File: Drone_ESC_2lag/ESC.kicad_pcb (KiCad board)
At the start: 4 copper layers, 107 parts, among them IC1 STSPIN32G4, J1 Conn_02x05_Odd_Even, J2 Conn_01x02_Pin, J3 Conn_01x02_Pin, J4 Conn_01x03_Pin, P1 USB_C_Plug_USB2.0, Q1 STL130N6F7, Q2 STL130N6F7, Q3 STL130N6F7, Q4 STL130N6F7, Q5 STL130N6F7, Q6 STL130N6F7, SW1 JS102011SAQN, Y1 24.000MHz

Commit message: delt igennem VS
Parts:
- moved IC1 2.98 mm to (171.1, 51.5)
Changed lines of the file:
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@@
 	(footprint "Drone_ESC:QFN50P900X900X100-65N-D"
 		(layer "F.Cu")
-		(at 168.5375 53.095)
+		(at 171.05 51.5)
 		(descr "STSPIN32G4")
 		(tags "Integrated Circuit")

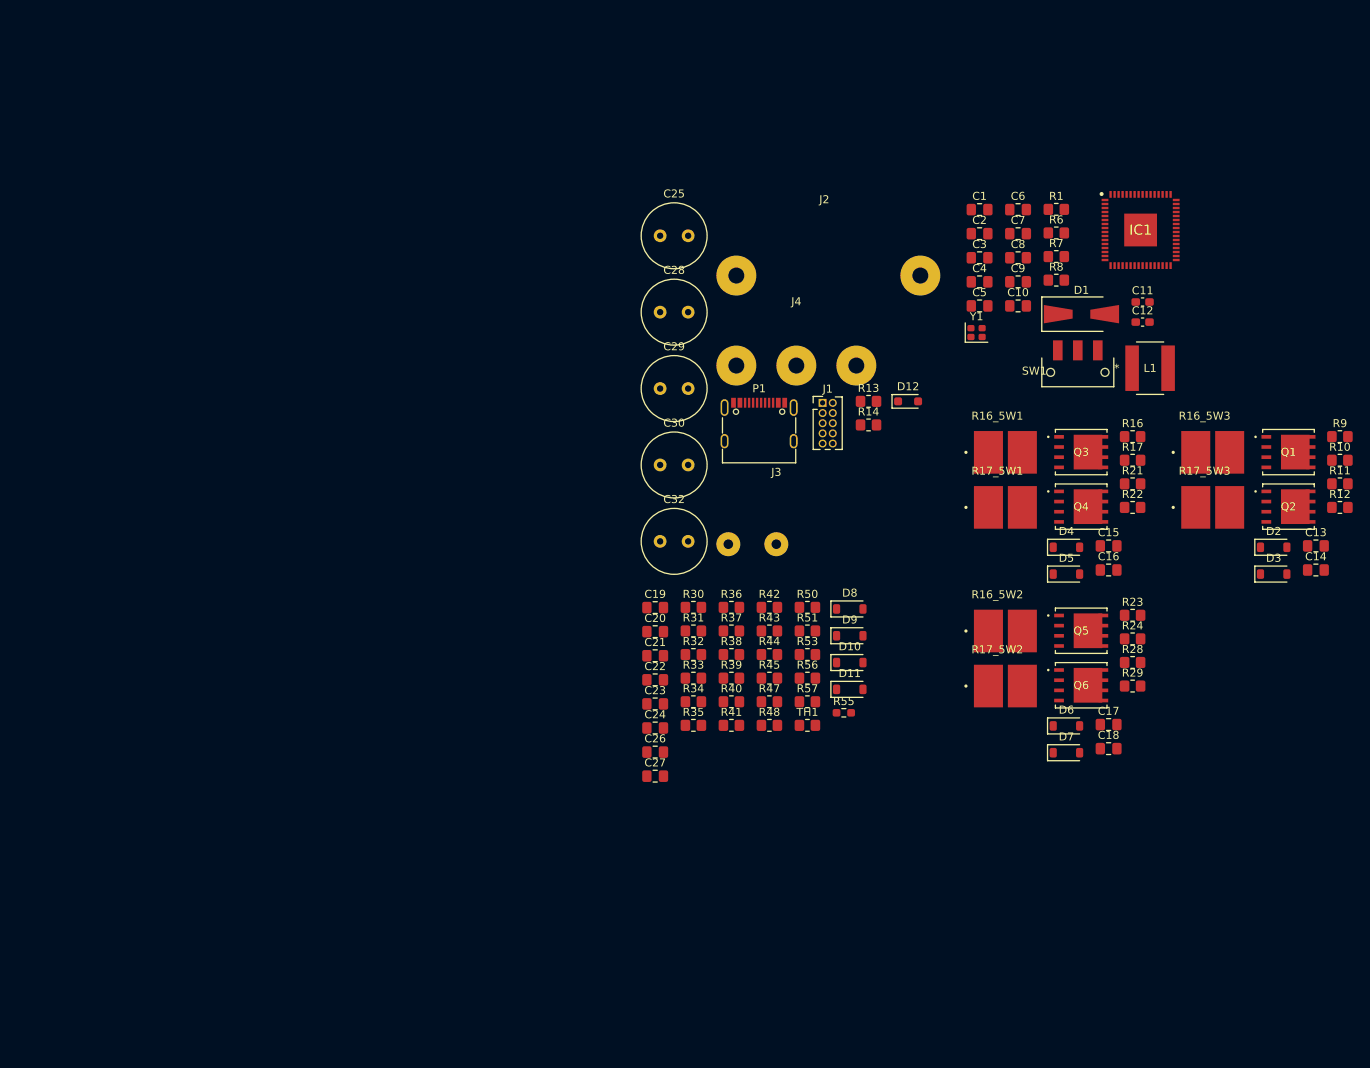
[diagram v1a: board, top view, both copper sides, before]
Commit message: Næsten færdig med PCB, retter fejl
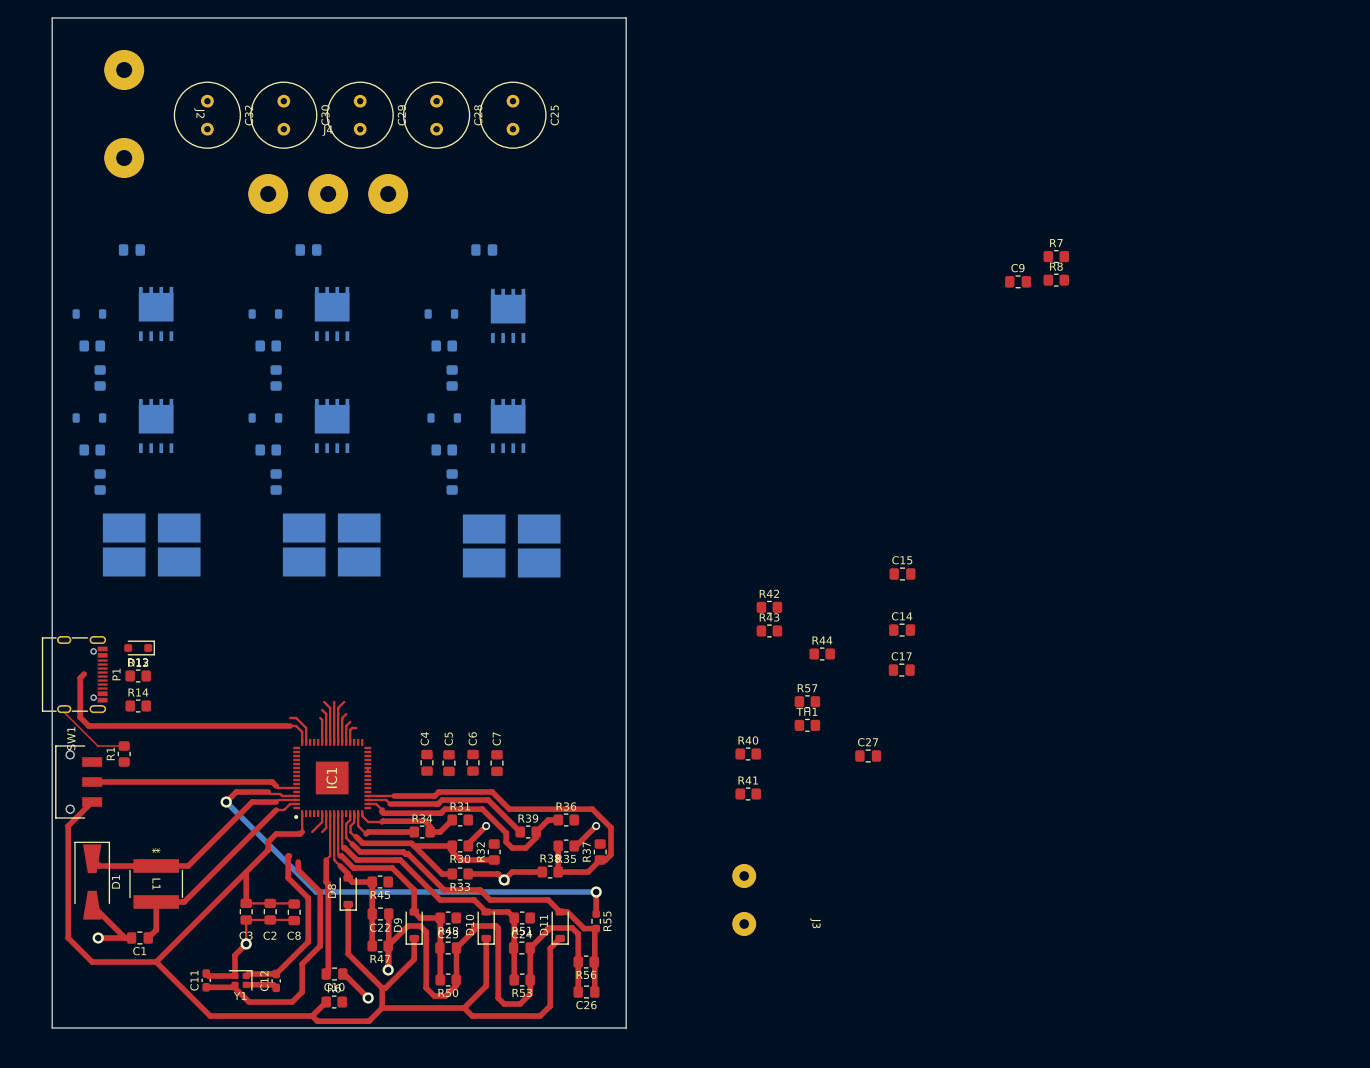
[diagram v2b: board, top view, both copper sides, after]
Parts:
- removed C19, C20, C21: 100nF, Capacitor_SMD:C_0805_2012Metric_Pad1.18x1.45mm_HandSolder
- removed J1: Conn_02x05_Odd_Even, Connector_PinHeader_1.27mm:PinHeader_2x05_P1.27mm_Vertical
- C13, C16, C18, D2, D3, D4, D5, D6, D7, Q1, Q2, Q3, Q4, Q5, Q6, R10, R11, R12, R16, R16_5W1, R16_5W2, R16_5W3, R17, R17_5W1, R17_5W2, R17_5W3, R21, R22, R23, R24, R28, R29, R9: moved to B.Cu
- moved C11 144.5 mm to (54.2, 145.3), turned to 90 degrees
- moved D1 142.6 mm to (40.0, 133.0), turned to -90 degrees
- moved L1 140.0 mm to (48.0, 133.3), turned to -90 degrees
- moved C1 138.9 mm to (46.0, 140.0), turned to 180 degrees
- moved C12 136.1 mm to (63.0, 145.4), turned to 90 degrees
- moved SW1 136.0 mm to (37.2, 120.5), turned to -90 degrees
- moved R1 134.9 mm to (44.0, 117.0), turned to 90 degrees
- moved R10 134.7 mm to (62.0, 66.0)
- moved R11 134.0 mm to (62.0, 79.0)
- moved R9 133.2 mm to (63.0, 70.0), turned to -90 degrees
- moved R12 133.0 mm to (63.0, 83.0), turned to -90 degrees
- moved R6 131.9 mm to (70.2, 148.0)
- moved C13 131.2 mm to (67.0, 54.0), turned to 180 degrees
- moved R16 130.5 mm to (40.0, 66.0)
- moved D3 130.2 mm to (61.6, 62.0)
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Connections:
- IC1 pad 49: PA13 -> unconnected-(IC1-PA13-Pad49)
- IC1 pad 50: PA14 -> unconnected-(IC1-PA14-Pad50)
- IC1 pad 51: PA15 -> unconnected-(IC1-PA15-Pad51)
- IC1 pad 54: PB3 -> unconnected-(IC1-PB3-Pad54)
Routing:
- net VDD: track 0.00 -> 166.8 mm
- net GND: track 0.00 -> 130.0 mm, vias 0 -> 5
- net VM: track 0.00 -> 63.2 mm, vias 0 -> 2
- net PA0: track 0.00 -> 47.2 mm
- net PA7: track 0.00 -> 46.6 mm
- net PC2: track 0.00 -> 37.3 mm
- net USB_D+: track 0.00 -> 35.4 mm
- net /STSPIN32G4 controller/PF1: track 0.00 -> 34.6 mm
- net PC1: track 0.00 -> 30.5 mm
- net PA5: track 0.00 -> 29.2 mm
- net PA1: track 0.00 -> 29.1 mm
- net /STSPIN32G4 controller/SW: track 0.00 -> 29.0 mm
- net VCC: track 0.00 -> 27.5 mm
- net Net-(IC1-PB8): track 0.00 -> 25.9 mm
- net /STSPIN32G4 controller/PF0: track 0.00 -> 24.3 mm
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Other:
- board outline added: 71.8 x 126.2 mm
- copper layers 4 -> 2

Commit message: Færdig PCB burde det være
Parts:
- removed C27: 33nF, Capacitor_SMD:C_0805_2012Metric_Pad1.18x1.45mm_HandSolder
- removed D12: PMEG45T10EXD-QX, Diode_SMD:D_SOD-323_HandSoldering
- removed P1: USB_C_Plug_USB2.0, Connector_USB:USB_C_Receptacle_G-Switch_GT-USB-7010ASV
- removed R13, R14: 5.1k, Resistor_SMD:R_0805_2012Metric_Pad1.20x1.40mm_HandSolder
- removed R57: 4.7k, Resistor_SMD:R_0805_2012Metric_Pad1.20x1.40mm_HandSolder
- removed SW1: JS102011SAQN, Switch:SW_JS102011SAQN
- removed TH1: Thermistor_NTC, Resistor_SMD:R_0805_2012Metric_Pad1.20x1.40mm_HandSolder
- added C19: 100nF, Capacitor_SMD:C_0805_2012Metric_Pad1.18x1.45mm_HandSolder, F.Cu at (41.0, 120.7)
- added J1: Conn_01x04, Connector_PinHeader_2.54mm:PinHeader_1x04_P2.54mm_Vertical, F.Cu at (38.2, 104.1)
- moved R7 124.3 mm to (53.0, 117.3)
- moved C9 121.8 mm to (52.7, 123.0), turned to 180 degrees
- moved R8 117.9 mm to (58.7, 117.3)
- moved C15 78.2 mm to (63.6, 103.3), turned to -90 degrees
- moved C14 66.4 mm to (74.9, 104.2), turned to 90 degrees
- moved C17 57.2 mm to (84.1, 103.2), turned to 90 degrees
- moved R44 39.6 mm to (94.5, 119.2), turned to 90 degrees
- moved C25 38.4 mm to (54.4, 38.9), turned to 90 degrees
- moved C32 38.4 mm to (92.6, 38.9), turned to 90 degrees
- moved J3 33.2 mm to (112.2, 110.2)
- moved R43 32.4 mm to (99.2, 121.8), turned to 180 degrees
- moved R42 28.1 mm to (103.8, 117.5), turned to 90 degrees
- moved R41 23.7 mm to (99.2, 115.5)
- moved R40 22.8 mm to (99.2, 118.8), turned to 180 degrees
- moved C28 19.4 mm to (64.0, 38.9), turned to 90 degrees
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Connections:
- IC1 pad 21: PC4 -> unconnected-(IC1-PC4-Pad21)
- IC1 pad 47: USB_D- -> unconnected-(IC1-PA11-Pad47)
- IC1 pad 48: USB_D+ -> unconnected-(IC1-PA12-Pad48)
- IC1 pad 49: unconnected-(IC1-PA13-Pad49) -> PA13
- IC1 pad 50: unconnected-(IC1-PA14-Pad50) -> PA14
- R1 pad 1: Net-(SW1-C) -> Net-(IC1-PB8)
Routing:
- net VDD: track 166.8 -> 371.6 mm, vias 0 -> 5
- net PHASE_V: track 5.36 -> 190.9 mm, vias 0 -> 3
- net GND: track 130.0 -> 281.9 mm, vias 5 -> 10
- net PHASE_U: track 4.26 -> 153.7 mm, vias 0 -> 2
- net PHASE_W: track 2.40 -> 136.2 mm, vias 0 -> 3
- net VM: track 63.2 -> 191.1 mm
- net GLS1: track 0.00 -> 97.3 mm, vias 0 -> 1
- net GLS2: track 0.00 -> 84.2 mm, vias 0 -> 1
- net VSHUNT1P: track 3.43 -> 80.6 mm, vias 1 -> 3
- net GHS1: track 3.15 -> 80.2 mm, vias 0 -> 1
- net GHS3: track 2.76 -> 63.5 mm, vias 0 -> 1
- net GHS2: track 5.05 -> 64.3 mm, vias 0 -> 1
- net VSHUNT2P: track 3.79 -> 60.4 mm
- net GLS3: track 0.00 -> 53.5 mm, vias 0 -> 1
- net PB10: track 0.00 -> 39.6 mm
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- added copper zone on B.Cu, net GND
- added copper zone on F.Cu, net GND
- added copper zone on B.Cu, net PHASE_U
- added copper zone on B.Cu, net PHASE_V
- added copper zone on B.Cu, net PHASE_W
- added copper zone on B.Cu, net VM
- added copper zone on B.Cu, net VSHUNT1P
- added copper zone on B.Cu, net VSHUNT2P
- added copper zone on B.Cu, net VSHUNT3P
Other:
- board size 71.8 x 126.2 mm -> 78.2 x 129 mm
